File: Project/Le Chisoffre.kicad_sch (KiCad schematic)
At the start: 117 parts, among them IC1 W25Q16JVUXIQ, J1 USB_C_Receptacle_USB2.0, SW1 boot, SW2 RotaryEncoder_Switch, U1 USBLC6-2SC6, U2 XC6206PxxxMR-Regulator_Linear, U3 RP2040, Y1 12MHz

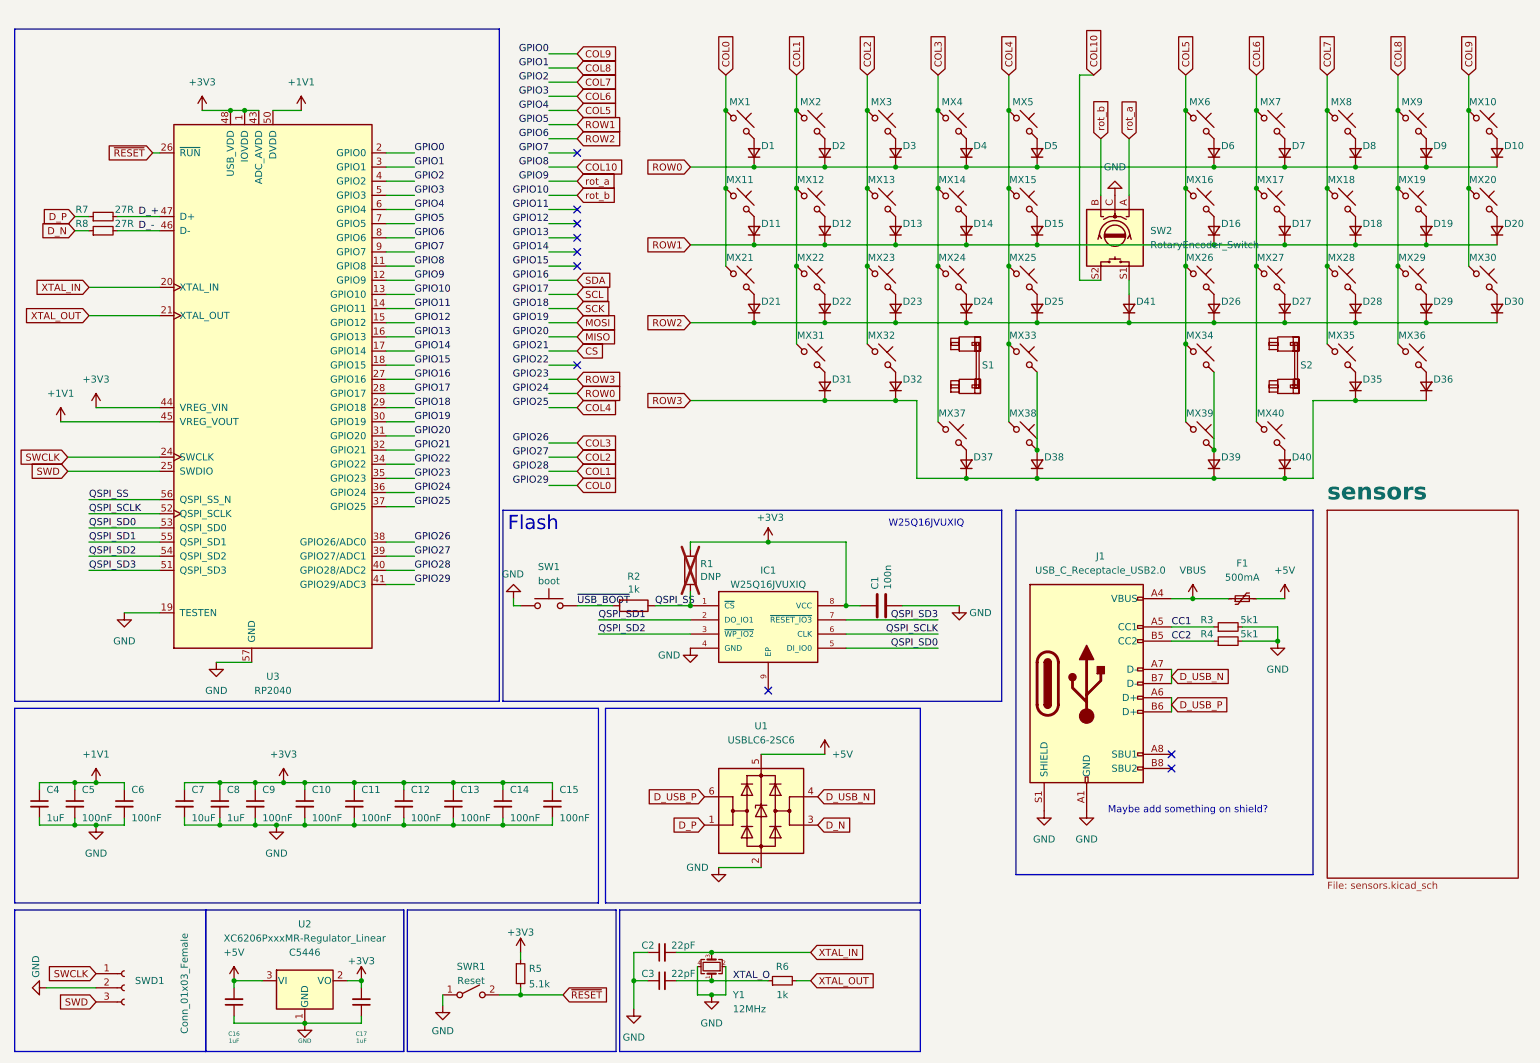
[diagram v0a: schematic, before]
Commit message: moved mcu, added extra encoder location
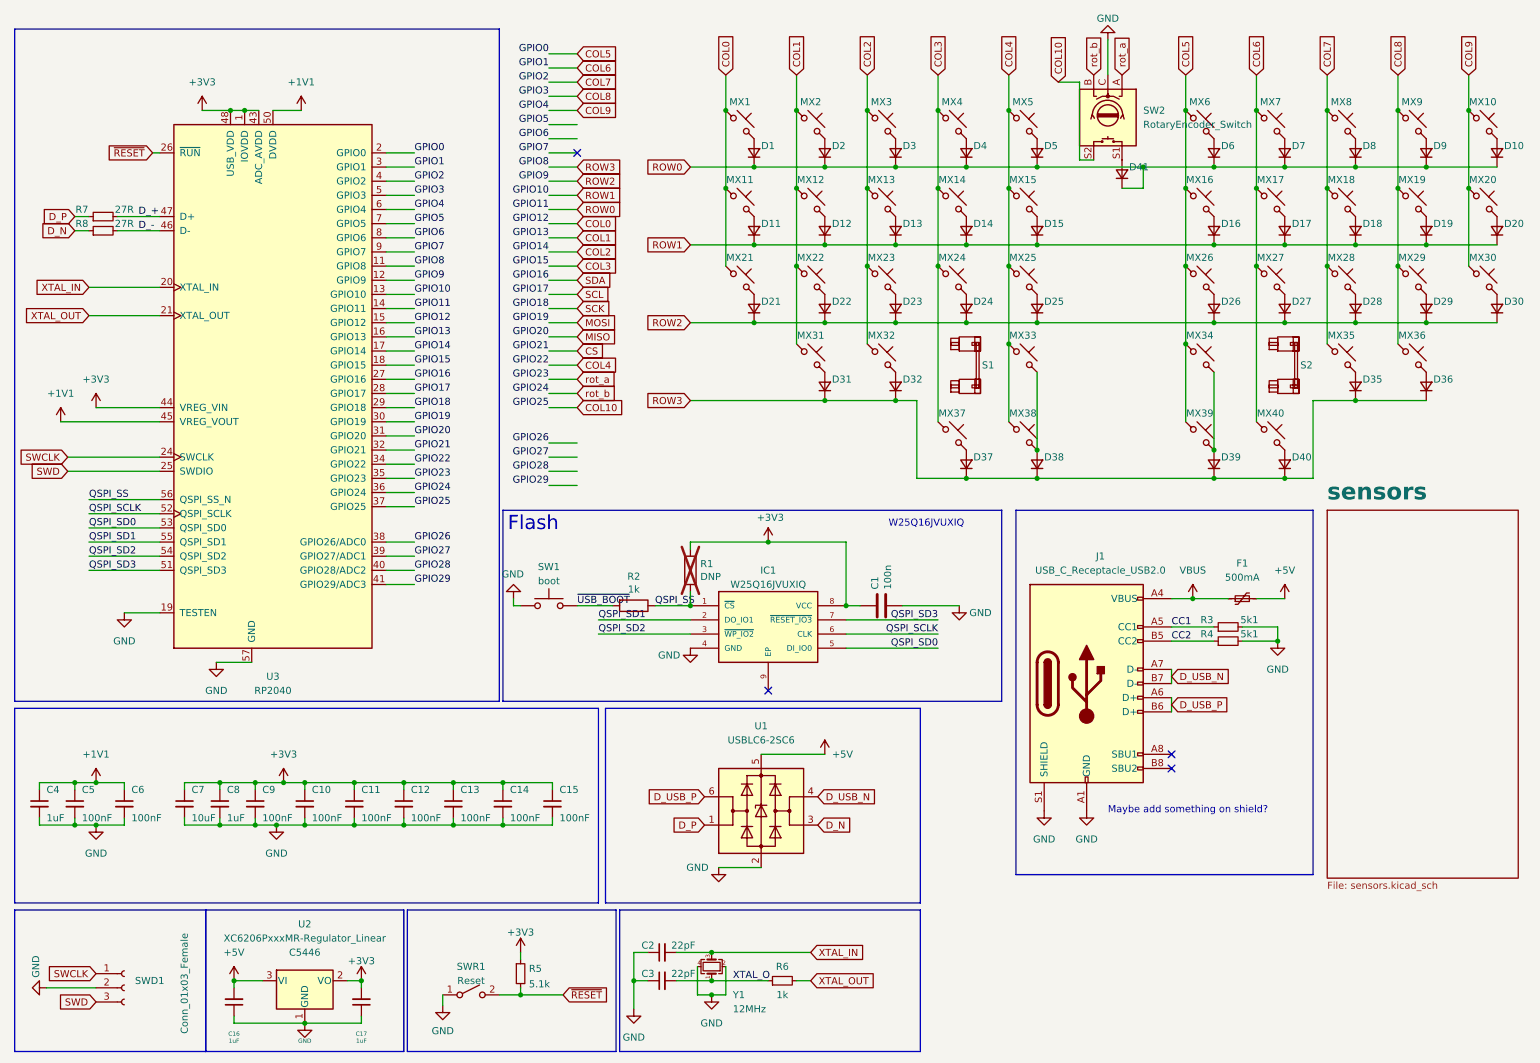
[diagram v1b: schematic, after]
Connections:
- net GPIO11 is gone; now on net ROW0: U3.14 (GPIO11)
- net GPIO12 is gone; now on net COL0: U3.15 (GPIO12)
- net GPIO13 is gone; now on net COL1: U3.16 (GPIO13)
- net GPIO14 is gone; now on net COL2: U3.17 (GPIO14)
- net GPIO15 is gone; now on net COL3: U3.18 (GPIO15)
- net GPIO22 is gone; now on net COL4: U3.34 (GPIO22)
- net COL0: no longer U3.41 (GPIO29/ADC3)
- net COL1: no longer U3.40 (GPIO28/ADC2)
- net COL10: now also U3.37 (GPIO25); no longer U3.11 (GPIO8)
- net COL2: no longer U3.39 (GPIO27/ADC1)
- net COL3: no longer U3.38 (GPIO26/ADC0)
- net COL4: no longer U3.37 (GPIO25)
- net COL5: now also U3.2 (GPIO0); no longer U3.6 (GPIO4)
- net COL6: now also U3.3 (GPIO1); no longer U3.5 (GPIO3)
- net COL8: now also U3.5 (GPIO3); no longer U3.3 (GPIO1)
- net COL9: now also U3.6 (GPIO4); no longer U3.2 (GPIO0)
- net ROW0: now also D41.1 (K); no longer U3.36 (GPIO24)
- net ROW1: now also U3.13 (GPIO10); no longer U3.7 (GPIO5)
- net ROW2: now also U3.12 (GPIO9); no longer D41.1 (K), U3.8 (GPIO6)
- net ROW3: now also U3.11 (GPIO8); no longer U3.35 (GPIO23)
- net rot_a: now also U3.35 (GPIO23); no longer U3.12 (GPIO9)
- net rot_b: now also U3.36 (GPIO24); no longer U3.13 (GPIO10)
- new net GPIO26: U3.38 (GPIO26/ADC0)
- new net GPIO27: U3.39 (GPIO27/ADC1)
- new net GPIO28: U3.40 (GPIO28/ADC2)
- new net GPIO29: U3.41 (GPIO29/ADC3)
- new net GPIO5: U3.7 (GPIO5)
- new net GPIO6: U3.8 (GPIO6)
- no-connect marks 10 -> 4
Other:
- moved on the sheet: D41, SW2

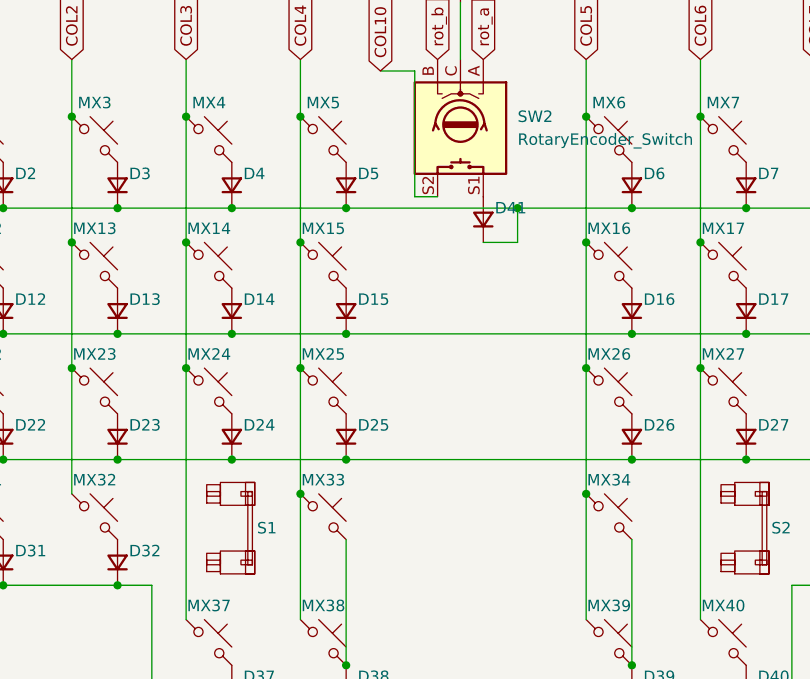
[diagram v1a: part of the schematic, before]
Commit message: clearing old files, symmetric edge cuts
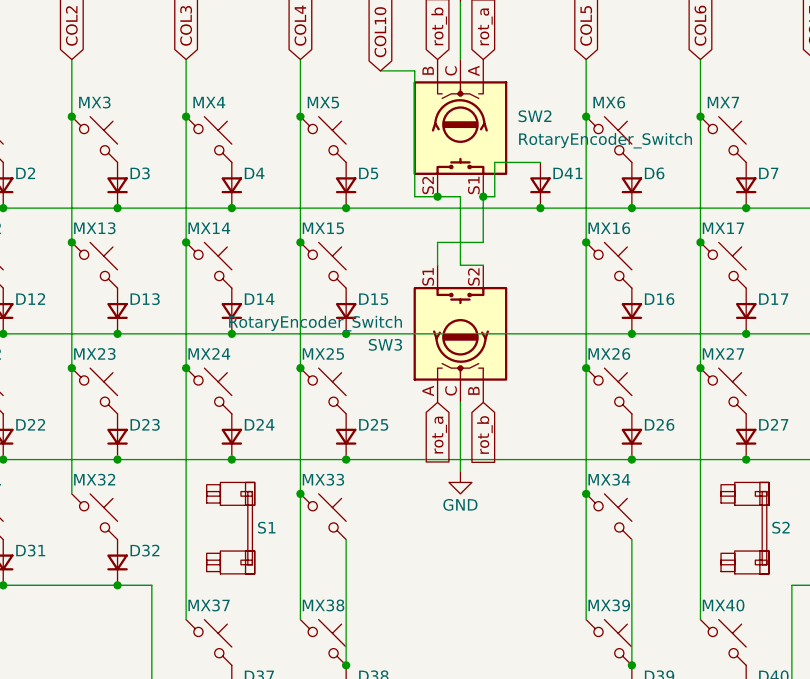
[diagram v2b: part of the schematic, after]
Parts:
- added SW3: RotaryEncoder_Switch, PCM_marbastlib-various:ROT_Alps_EC11E-Switch, symbol Device:RotaryEncoder_Switch
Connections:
- net COL10: now also SW3.S2
- net GND: now also SW3.C
- net rot_a: now also SW3.A
- net rot_b: now also SW3.B
- net at D41.2 (A), SW2.S1: now also SW3.S1
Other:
- moved on the sheet: D41

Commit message: moving things
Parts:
- added D41: D_Small, Diode_SMD:D_SOD-123F, symbol Device:D_Small
- renumbered D41 to D33
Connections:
- net ROW1: now also D41.1 (K)
- net at D33.2 (A), SW2.S1: no longer SW3.S1
- new net: D41.2 (A), SW3.S1
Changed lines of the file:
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@@
 	)
 	(junction
-		(at 24.13 156.21)
+		(at 218.44 52.07)
 		(diameter 0)
 		(color 0 0 0 0)
 	)
 	(junction
-		(at 166.37 27.94)
+		(at 24.13 156.21)
 		(diameter 0)
 		(color 0 0 0 0)
 	)
 	(junction
-		(at 171.45 66.04)
+		(at 166.37 27.94)
 		(diameter 0)
 		(color 0 0 0 0)
 	)
 	(junction
-		(at 212.09 36.83)
+		(at 171.45 66.04)
 		(diameter 0)
 		(color 0 0 0 0)
@@
 	(wire
 		(pts
+			(xy 218.44 52.07) (xy 228.6 52.07)
+		)
+		(stroke
+			(width 0)
+			(type default)
+		)
+	)
+	(wire
+		(pts
 			(xy 140.97 186.69) (xy 138.43 186.69)
 		)
@@
 	(wire
 		(pts
-			(xy 207.01 41.91) (xy 212.09 41.91)
+			(xy 246.38 80.01) (xy 246.38 93.98)
 		)
 		(stroke
@@
 	(wire
 		(pts
-			(xy 246.38 80.01) (xy 246.38 93.98)
+			(xy 246.38 80.01) (xy 254 80.01)
 		)
 		(stroke
@@
 	(wire
 		(pts
-			(xy 246.38 80.01) (xy 254 80.01)
+			(xy 204.47 22.86) (xy 204.47 36.83)
 		)
 		(stroke
@@
 	(wire
 		(pts
-			(xy 204.47 22.86) (xy 204.47 36.83)
+			(xy 218.44 43.18) (xy 207.01 43.18)
 		)
 		(stroke
@@
 	(wire
 		(pts
+			(xy 207.01 43.18) (xy 207.01 44.45)
+		)
+		(stroke
+			(width 0)
+			(type default)
+		)
+	)
+	(wire
+		(pts
 			(xy 254 80.01) (xy 266.7 80.01)
 		)
@@
 	(wire
 		(pts
-			(xy 196.85 52.07) (xy 228.6 52.07)
+			(xy 196.85 52.07) (xy 218.44 52.07)
 		)
 		(stroke
@@
 	(wire
 		(pts
+			(xy 218.44 46.99) (xy 218.44 43.18)
+		)
+		(stroke
+			(width 0)
+			(type default)
+		)
+	)
+	(wire
+		(pts
 			(xy 162.56 105.41) (xy 162.56 116.84)
 		)
@@
 	(wire
 		(pts
-			(xy 212.09 36.83) (xy 212.09 41.91)
-		)
-		(stroke
-			(width 0)
-			(type default)
-		)
-	)
-	(wire
-		(pts
-			(xy 207.01 44.45) (xy 207.01 41.91)
-		)
-		(stroke
-			(width 0)
-			(type default)
-		)
-	)
-	(wire
-		(pts
 			(xy 80.01 76.2) (xy 85.09 76.2)
 		)
@@
 		(on_board yes)
 		(dnp no)
-		(property "Reference" "D41"
+		(property "Reference" "D33"
 			(at 219.71 34.29 90)
 			(effects
@@
 			(project ""
 				(path "/1b359c20-7ce0-4923-93db-3e704c7c3bfa"
-					(reference "D41")
+					(reference "D33")
 					(unit 1)
 				)
@@
 					(unit 1)
 				)
+			)
+		)
+	)
+	(symbol
+		(lib_id "Device:D_Small")
+		(at 218.44 49.53 90)
+		(unit 1)
+		(exclude_from_sim no)
+		(in_bom yes)
+		(on_board yes)
+		(dnp no)
+		(property "Reference" "D41"
+			(at 219.71 48.26 90)
+			(effects
+				(font
+					(size 1.27 1.27)
+				)
+				(justify right)
+			)
+		)
+		(property "Value" "D_Small"
+			(at 220.98 50.7999 90)
+			(effects
+				(font
+					(size 1.27 1.27)
+				)
+				(justify right)
+				(hide yes)
+			)
+		)
+		(property "Footprint" "Diode_SMD:D_SOD-123F"
+			(at 218.44 49.53 90)
+			(effects
+				(font
+					(size 1.27 1.27)
+				)
+				(hide yes)
+			)
+		)
+		(property "Datasheet" "~"
+			(at 218.44 49.53 90)
+			(effects
+				(font
+					(size 1.27 1.27)
+				)
+				(hide yes)
+			)
+		)
+		(property "Description" "Diode, small symbol"
+			(at 218.44 49.53 0)
+			(effects
+				(font
+					(size 1.27 1.27)
+				)
+				(hide yes)
+			)
+		)
+		(property "Sim.Device" "D"
+			(at 218.44 49.53 0)
+			(effects
+				(font
+					(size 1.27 1.27)
+				)
+				(hide yes)
+			)
+		)
+		(property "Sim.Pins" "1=K 2=A"
+			(at 218.44 49.53 0)
+			(effects
+				(font
+					(size 1.27 1.27)
+				)
+				(hide yes)
+			)
+		)
+		(pin "1"
+		)
+		(pin "2"
+		)
+		(instances
+			(project "Le Chisoffre"
+				(path "/1b359c20-7ce0-4923-93db-3e704c7c3bfa"
+					(reference "D41")
+					(unit 1)
+				)
